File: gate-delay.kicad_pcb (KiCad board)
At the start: 2 copper layers, 11 parts, among them J1 Conn_02x05_Odd_Even

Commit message: feat: v0 pcb layed out
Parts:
- added C3: 1u box, Capacitor_THT:C_Rect_L7.2mm_W5.5mm_P5.00mm_FKS2_FKP2_MKS2_MKP2, B.Cu at (121.1, 93.5)
- added C4: 100n, Capacitor_SMD:C_0805_2012Metric, F.Cu at (130.3, 96.2)
- added D3: 1N4148, Diode_SMD:D_SOD-323_HandSoldering, F.Cu at (138.4, 86.0)
- added D4: 1N4148, Diode_SMD:D_SOD-323_HandSoldering, F.Cu at (129.2, 85.7)
- added D5: LED_GREEN, LED_THT:LED_D3.0mm, F.Cu at (114.3, 95.7)
- added H5: input, Eurorack:Mech-AudioJack-Hole-Input-Gate, F.Cu at (103.3, 118.1)
- added H6: output, Eurorack:Mech-AudioJack-Hole-Output-Gate, F.Cu at (115.5, 118.3)
- added H7: slew, Eurorack:Mech-AudioJack-Hole-Output-CV, F.Cu at (103.3, 129.5)
- added H8: delay, Eurorack:Mech-Potentiometer-Hole_level_90deg, F.Cu at (148.8, 123.7)
- added H9: led, Eurorack:Mech-LED-Hole-3mm-Bezel, F.Cu at (115.5, 129.3)
- added J2: gate_in, Eurorack:AudioJack2_Tayda_A-2566, F.Cu at (103.3, 84.5)
- added J3: gate_out, Eurorack:AudioJack2_Tayda_A-2566, F.Cu at (115.5, 84.5)
- added J4: slew_out, Eurorack:AudioJack2_Tayda_A-2566, F.Cu at (103.3, 95.7)
- added Q1: BCM847, Package_SO:TSOP-6_1.65x3.05mm_P0.95mm, F.Cu at (137.5, 89.3)
- added Q2: BSS84, Package_TO_SOT_SMD:SOT-23, F.Cu at (136.1, 93.5)
- added Q3: MMBF170, Package_TO_SOT_SMD:SOT-23, F.Cu at (139.9, 93.5)
- added R10: 1K, Resistor_SMD:R_0805_2012Metric, F.Cu at (128.2, 82.0)
- added R11: 10K, Resistor_SMD:R_0805_2012Metric, F.Cu at (124.2, 81.5)
- added R12: 1K, Resistor_SMD:R_0805_2012Metric, F.Cu at (112.0, 94.2)
- added R13: 1K, Resistor_SMD:R_0805_2012Metric, F.Cu at (124.2, 86.6)
- added R14: 1K, Resistor_SMD:R_0805_2012Metric, F.Cu at (109.6, 99.2)
- added R3: 1K, Resistor_SMD:R_0805_2012Metric, F.Cu at (136.0, 83.3)
- added R4: 22K, Resistor_SMD:R_0805_2012Metric, F.Cu at (140.0, 83.3)
- added R5: 22K, Resistor_SMD:R_0805_2012Metric, F.Cu at (141.6, 89.3)
- added R6: 1K, Resistor_SMD:R_0805_2012Metric, F.Cu at (136.1, 97.0)
- added R7: 1K, Resistor_SMD:R_0805_2012Metric, F.Cu at (139.9, 97.0)
- added R8: 110K, Resistor_SMD:R_0805_2012Metric, F.Cu at (128.2, 90.6)
- added R9: 22K, Resistor_SMD:R_0805_2012Metric, F.Cu at (124.2, 90.6)
- added RV1: A1M, Eurorack:Potentiometer_RV16AF-41-15R1, F.Cu at (148.8, 90.1)
- added U1: TL072, Package_SO:SOIC-8_3.9x4.9mm_P1.27mm, F.Cu at (125.7, 96.2)
- moved H4 159.6 mm to (152.3, 140.8)
- moved H2 143.6 mm to (152.3, 107.1)
- moved H3 131.9 mm to (102.0, 140.8)
- moved H1 111.0 mm to (101.5, 107.3)
- moved J1 106.2 mm to (151.1, 95.2), turned to 0 degrees
- moved D1 98.0 mm to (146.8, 94.7), turned to -90 degrees
- moved R2 96.9 mm to (147.8, 91.4), turned to 0 degrees
- moved C1 95.1 mm to (143.3, 97.7), turned to 0 degrees
- moved R1 95.0 mm to (147.8, 88.8), turned to 0 degrees
- moved D2 90.9 mm to (146.8, 85.5), turned to -90 degrees
- moved C2 87.0 mm to (145.7, 82.2), turned to 180 degrees
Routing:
- net GND: track 41.0 -> 96.4 mm, vias 0 -> 3
- net +12V: track 14.2 -> 61.8 mm, vias 0 -> 3
- net /GATE_IN': track 0.00 -> 36.5 mm
- net -12V: track 14.7 -> 49.1 mm, vias 0 -> 1
- net Net-(U1A-+): track 0.00 -> 26.3 mm
- net Net-(D5-A): track 0.00 -> 22.3 mm, vias 0 -> 1
- net Net-(U1B--): track 0.00 -> 18.5 mm
- net Net-(R6-Pad1): track 0.00 -> 15.9 mm, vias 0 -> 1
- net Net-(D4-K): track 0.00 -> 14.6 mm
- net /GATE_OUT': track 0.00 -> 9.40 mm
- net Net-(Q1A-C1): track 0.00 -> 8.59 mm
- net Net-(D4-A): track 0.00 -> 7.45 mm
- net Net-(D3-K): track 0.00 -> 7.29 mm
- net Net-(R10-Pad1): track 0.00 -> 6.57 mm
- net /SLEW_OUT': track 0.00 -> 6.44 mm
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- added copper zone on B.Cu, net /FACE
- added copper zone on F.Cu, net /FACE
- added copper zone on B.Cu, net GND
- added copper zone on F.Cu, net GND
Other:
- board outline added: 60.6 x 64.7 mm
- board text added: "gate delay"
- board text added: "thismatters/gate-delay/v0"

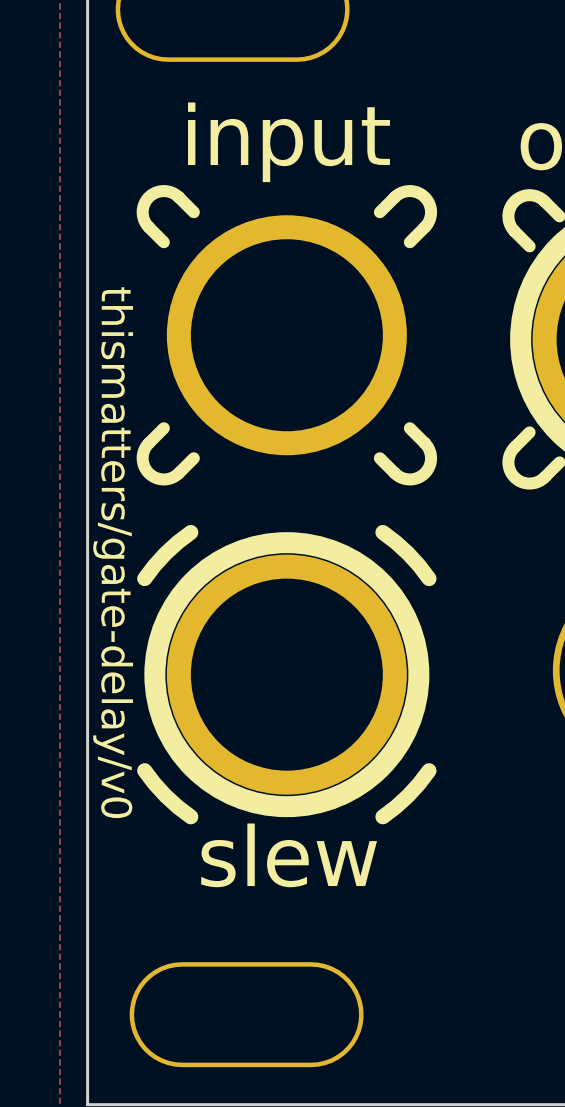
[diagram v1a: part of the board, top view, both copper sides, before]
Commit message: v1 ready (uses the v0 board)
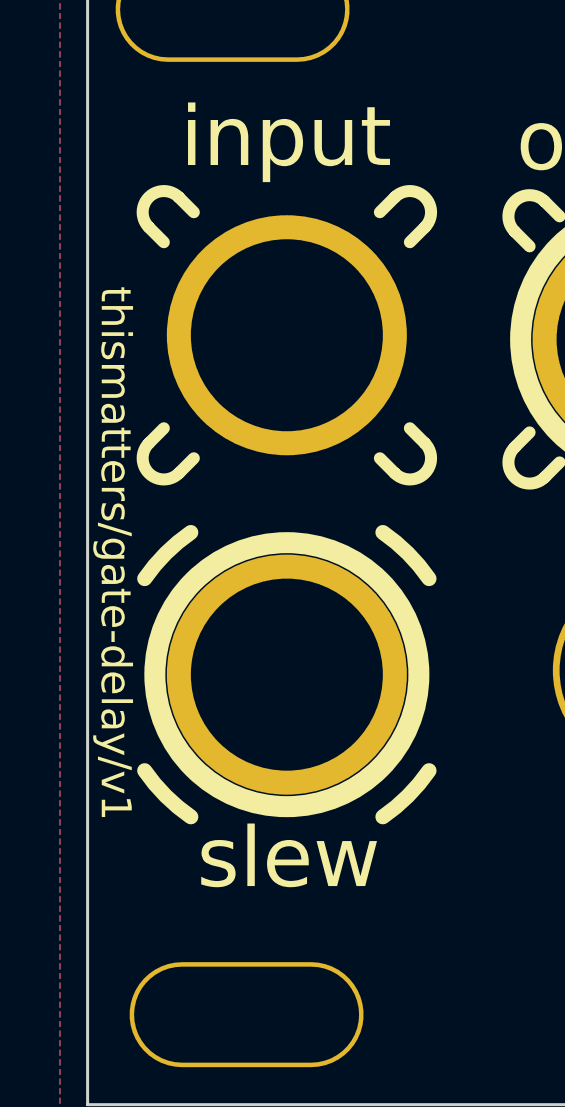
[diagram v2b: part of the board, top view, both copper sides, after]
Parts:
- R8: value 110K -> 22K
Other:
- board text added: "thismatters/gate-delay/v1"
- board text removed: "thismatters/gate-delay/v0"
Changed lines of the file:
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@@
         (effects (font (size 1 1) (thickness 0.15)))
     )
-    (fp_text value "110K" (at 0 1.65) (layer "F.Fab")
+    (fp_text value "22K" (at 0 1.65) (layer "F.Fab")
         (effects (font (size 1 1) (thickness 0.15)))
     )
@@
     (effects (font (size 1 1) (thickness 0.15)) (justify bottom mirror))
   )
-  (gr_text "thismatters/gate-delay/v0" (at 131.028 80.718) (layer "B.SilkS")
+  (gr_text "thismatters/gate-delay/v1" (at 131.028 80.718) (layer "B.SilkS")
     (effects (font (size 1 1) (thickness 0.15)) (justify bottom mirror))
   )
@@
     (effects (font (size 4 3) (thickness 0.45)) (justify bottom))
   )
-  (gr_text "thismatters/gate-delay/v0" (at 97.05 125.418 -90) (layer "F.SilkS")
+  (gr_text "thismatters/gate-delay/v1" (at 97.05 125.418 270) (layer "F.SilkS")
     (effects (font (size 1 1) (thickness 0.15)) (justify bottom))
   )
